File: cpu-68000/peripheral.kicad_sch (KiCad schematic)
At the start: 57 parts, among them J502 DB9_Male_MountingHoles, J503 Conn_02x03_Odd_Even, SW501 SW_DIP_x05, SW502 Blue, SW503 Black, U501 74HC2G14, U502 PCA9543A, U503 XR68C681, U504 PCF8584, U505 DS1744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

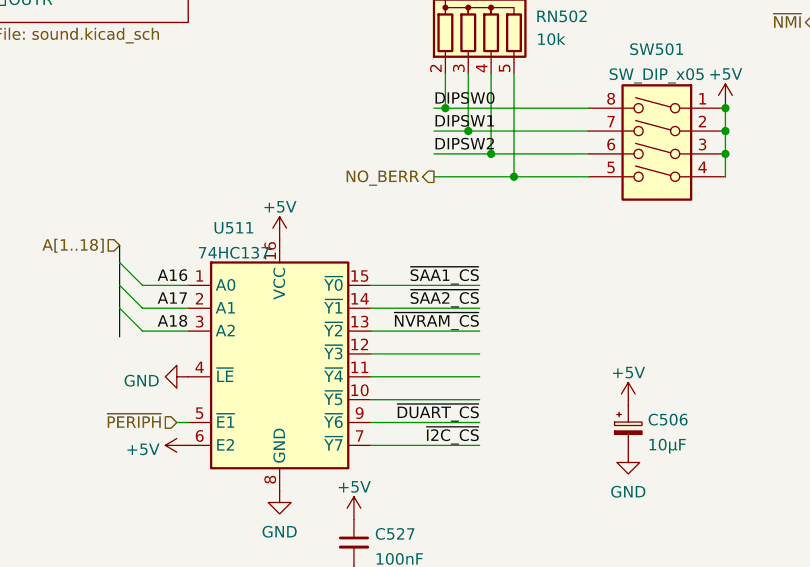
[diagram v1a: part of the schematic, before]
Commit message: Replaced half the RAM for flash (boot ROM)
Squashed commit of the following:

commit 629e5dca317ab35f390a35a51af997ba405215d5
Author: Tristan Seifert <tristan@tseifert.me>
Date:   Tue Nov 30 18:31:19 2021 -0800

    Added high byte flash chip

    - Replaced one of the RAMs with another flash, so that we can have
      on-board boot ROM of 1M. It'll have to be programmed in system (or
      very flimsily out of system before soldering) so a switch to remap the
      flash to elsehwere in the address space is provided (formerly BERR
      inhibit switch)

commit c59845a042d2b99cf0eb5e3cdf44f56cd0b06346
Author: Tristan Seifert <tristan@tseifert.me>
Date:   Tue Nov 30 16:27:37 2021 -0800

    Fixed address line routing to match flash chip

    - While the routing is slightly simplified by having the address lines
      not line up, we instead have the address pins match up so the
      programming logic is simplified (flash can only be written in sectors)

commit c1633293517c92d21a59f13bdb24d4da193bf248
Author: Tristan Seifert <tristan@tseifert.me>
Date:   Tue Nov 30 16:09:11 2021 -0800

    Switched one of the RAMs for a flash chip

    - This should allow us to have a boot ROM on the board; it will need to
      be bootstraped and programmed in-system by some external jig though.

commit 7dedf6a3a6ad9d60be3a7b8b35cf8e3edec37929
Author: Tristan Seifert <tristan@tseifert.me>
Date:   Tue Nov 30 15:02:12 2021 -0800

    Created footprints for PGA 68000

    - Also reworked the address decoding for peripherals so all peripherals
      that generate their own /DTACK are on the same half of the peripheral
      address space
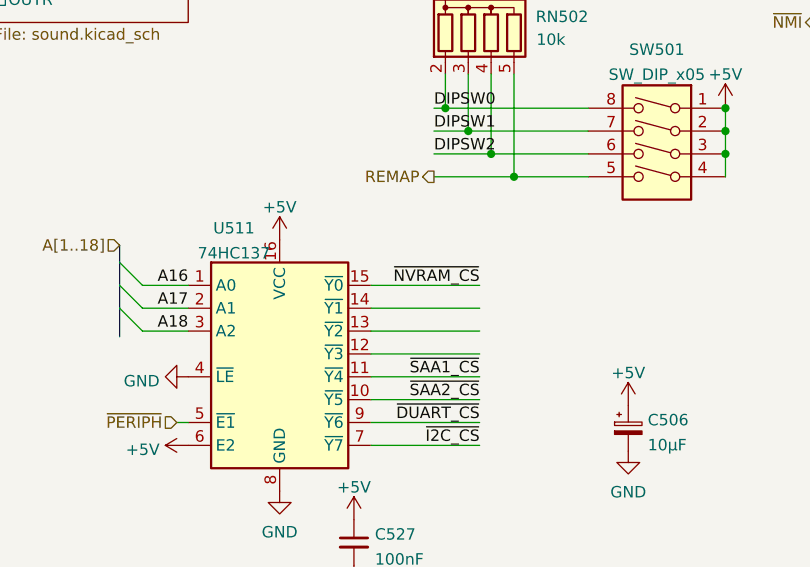
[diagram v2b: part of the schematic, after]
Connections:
- net ~{NVRAM_CS}: now also U511.15 (~{Y0}); no longer U511.13 (~{Y2})
- net ~{SAA1_CS}: now also U511.11 (~{Y4}); no longer U511.15 (~{Y0})
- net ~{SAA2_CS}: now also U511.10 (~{Y5}); no longer U511.14 (~{Y1})
- net NO_BERR renamed REMAP
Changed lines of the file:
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@@
-(kicad_sch (version 20210621) (generator eeschema)
+(kicad_sch (version 20211123) (generator eeschema)
   (paper "A4")
-  (junction (at 156.21 147.955) (diameter 0) (color 0 0 0 0))
-  (junction (at 236.855 124.46) (diameter 0) (color 0 0 0 0))
-  (junction (at 179.705 145.415) (diameter 0) (color 0 0 0 0))
-  (junction (at 170.18 94.615) (diameter 0) (color 0 0 0 0))
-  (junction (at 41.275 151.13) (diameter 0) (color 0 0 0 0))
-  (junction (at 45.72 69.85) (diameter 0) (color 0 0 0 0))
-  (junction (at 45.72 64.77) (diameter 0) (color 0 0 0 0))
-  (junction (at 227.33 124.46) (diameter 0) (color 0 0 0 0))
-  (junction (at 151.13 142.875) (diameter 0) (color 0 0 0 0))
-  (junction (at 212.725 124.46) (diameter 0) (color 0 0 0 0))
-  (junction (at 225.425 99.3624) (diameter 0) (color 0 0 0 0))
-  (junction (at 170.18 99.695) (diameter 0) (color 0 0 0 0))
-  (junction (at 212.725 130.81) (diameter 0) (color 0 0 0 0))
-  (junction (at 77.47 176.53) (diameter 0) (color 0 0 0 0))
-  (junction (at 21.59 81.28) (diameter 0) (color 0 0 0 0))
-  (junction (at 34.925 126.365) (diameter 0) (color 0 0 0 0))
-  (junction (at 179.705 142.875) (diameter 0) (color 0 0 0 0))
-  (junction (at 227.33 140.335) (diameter 0) (color 0 0 0 0))
-  (junction (at 212.725 114.3) (diameter 0) (color 0 0 0 0))
-  (junction (at 41.275 146.05) (diameter 0) (color 0 0 0 0))
-  (junction (at 148.59 140.335) (diameter 0) (color 0 0 0 0))
-  (junction (at 75.565 80.01) (diameter 0) (color 0 0 0 0))
-  (junction (at 151.13 20.955) (diameter 0) (color 0 0 0 0))
-  (junction (at 153.67 145.415) (diameter 0) (color 0 0 0 0))
-  (junction (at 41.275 148.59) (diameter 0) (color 0 0 0 0))
-  (junction (at 41.275 156.21) (diameter 0) (color 0 0 0 0))
-  (junction (at 77.47 181.61) (diameter 0) (color 0 0 0 0))
-  (junction (at 77.47 186.69) (diameter 0) (color 0 0 0 0))
-  (junction (at 273.685 45.72) (diameter 0) (color 0 0 0 0))
-  (junction (at 212.725 140.335) (diameter 0) (color 0 0 0 0))
-  (junction (at 41.275 153.67) (diameter 0) (color 0 0 0 0))
-  (junction (at 179.705 140.335) (diameter 0) (color 0 0 0 0))
-  (junction (at 146.05 20.955) (diameter 0) (color 0 0 0 0))
+  (junction (at 41.275 148.59) (diameter 0) (color 0 0 0 0)
+  )
+  (junction (at 77.47 181.61) (diameter 0) (color 0 0 0 0)
+  )
+  (junction (at 212.725 124.46) (diameter 0) (color 0 0 0 0)
+  )
+  (junction (at 21.59 81.28) (diameter 0) (color 0 0 0 0)
+  )
+  (junction (at 77.47 176.53) (diameter 0) (color 0 0 0 0)
+  )
+  (junction (at 45.72 64.77) (diameter 0) (color 0 0 0 0)
+  )
+  (junction (at 151.13 20.955) (diameter 0) (color 0 0 0 0)
+  )
+  (junction (at 212.725 130.81) (diameter 0) (color 0 0 0 0)
+  )
+  (junction (at 225.425 99.3624) (diameter 0) (color 0 0 0 0)
+  )
+  (junction (at 236.855 124.46) (diameter 0) (color 0 0 0 0)
+  )
+  (junction (at 170.18 94.615) (diameter 0) (color 0 0 0 0)
+  )
+  (junction (at 75.565 80.01) (diameter 0) (color 0 0 0 0)
+  )
+  (junction (at 212.725 140.335) (diameter 0) (color 0 0 0 0)
+  )
+  (junction (at 179.705 142.875) (diameter 0) (color 0 0 0 0)
+  )
+  (junction (at 45.72 69.85) (diameter 0) (color 0 0 0 0)
+  )
+  (junction (at 170.18 99.695) (diameter 0) (color 0 0 0 0)
+  )
+  (junction (at 273.685 45.72) (diameter 0) (color 0 0 0 0)
+  )
+  (junction (at 41.275 146.05) (diameter 0) (color 0 0 0 0)
+  )
+  (junction (at 153.67 145.415) (diameter 0) (color 0 0 0 0)
+  )
+  (junction (at 227.33 140.335) (diameter 0) (color 0 0 0 0)
+  )
+  (junction (at 77.47 186.69) (diameter 0) (color 0 0 0 0)
+  )
+  (junction (at 156.21 147.955) (diameter 0) (color 0 0 0 0)
+  )
+  (junction (at 148.59 140.335) (diameter 0) (color 0 0 0 0)
+  )
+  (junction (at 34.925 126.365) (diameter 0) (color 0 0 0 0)
+  )
+  (junction (at 41.275 151.13) (diameter 0) (color 0 0 0 0)
+  )
+  (junction (at 179.705 145.415) (diameter 0) (color 0 0 0 0)
+  )
+  (junction (at 146.05 20.955) (diameter 0) (color 0 0 0 0)
+  )
+  (junction (at 41.275 153.67) (diameter 0) (color 0 0 0 0)
+  )
+  (junction (at 41.275 156.21) (diameter 0) (color 0 0 0 0)
+  )
+  (junction (at 179.705 140.335) (diameter 0) (color 0 0 0 0)
+  )
+  (junction (at 151.13 142.875) (diameter 0) (color 0 0 0 0)
+  )
+  (junction (at 212.725 114.3) (diameter 0) (color 0 0 0 0)
+  )
+  (junction (at 227.33 124.46) (diameter 0) (color 0 0 0 0)
+  )
   (bus_entry (at 132.715 41.275) (size 2.54 -2.54)
     (stroke (width 0) (type default) (color 0 0 0 0))
@@
     (effects (font (size 1.27 1.27)) (justify right bottom))
   )
-  (label "~{NVRAM_CS}" (at 152.4 165.1 180)
+  (label "~{NVRAM_CS}" (at 152.4 160.02 180)
     (effects (font (size 1.27 1.27)) (justify right bottom))
   )
@@
     (effects (font (size 1.27 1.27)) (justify right bottom))
   )
-  (label "~{SAA2_CS}" (at 152.4 162.56 180)
+  (label "~{SAA2_CS}" (at 152.4 172.72 180)
     (effects (font (size 1.27 1.27)) (justify right bottom))
   )
@@
     (effects (font (size 1.27 1.27)) (justify right bottom))
   )
-  (label "~{SAA1_CS}" (at 152.4 160.02 180)
+  (label "~{SAA1_CS}" (at 152.4 170.18 180)
     (effects (font (size 1.27 1.27)) (justify right bottom))
   )
@@
     (effects (font (size 1.27 1.27)) (justify right))
   )
-  (hierarchical_label "NO_BERR" (shape output) (at 147.32 147.955 180)
-    (effects (font (size 1.27 1.27)) (justify right))
-  )
+  (hierarchical_label "REMAP" (shape output) (at 147.32 147.955 180)
+    (effects (font (size 1.27 1.27)) (justify right))
+  )

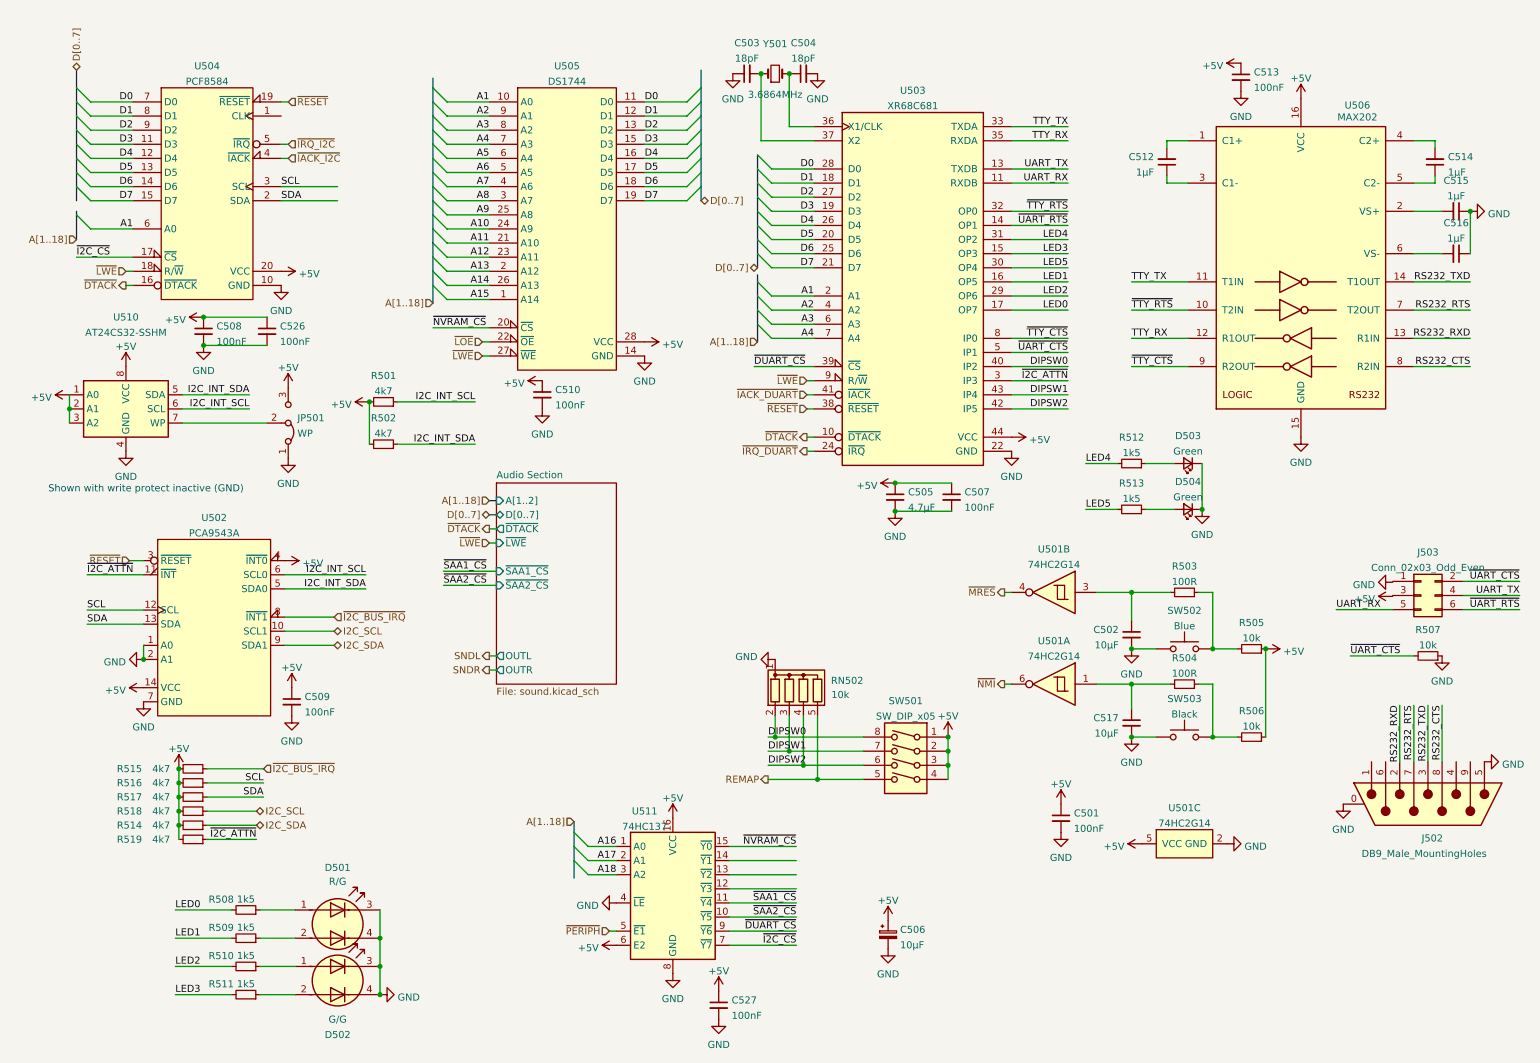
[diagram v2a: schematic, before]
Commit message: Minor cleanup of CPU board
- Switched out of stock 2 bit level shifters for 8 bit part we already
  have; this means that the function codes will be buffered along with
  all other signals.
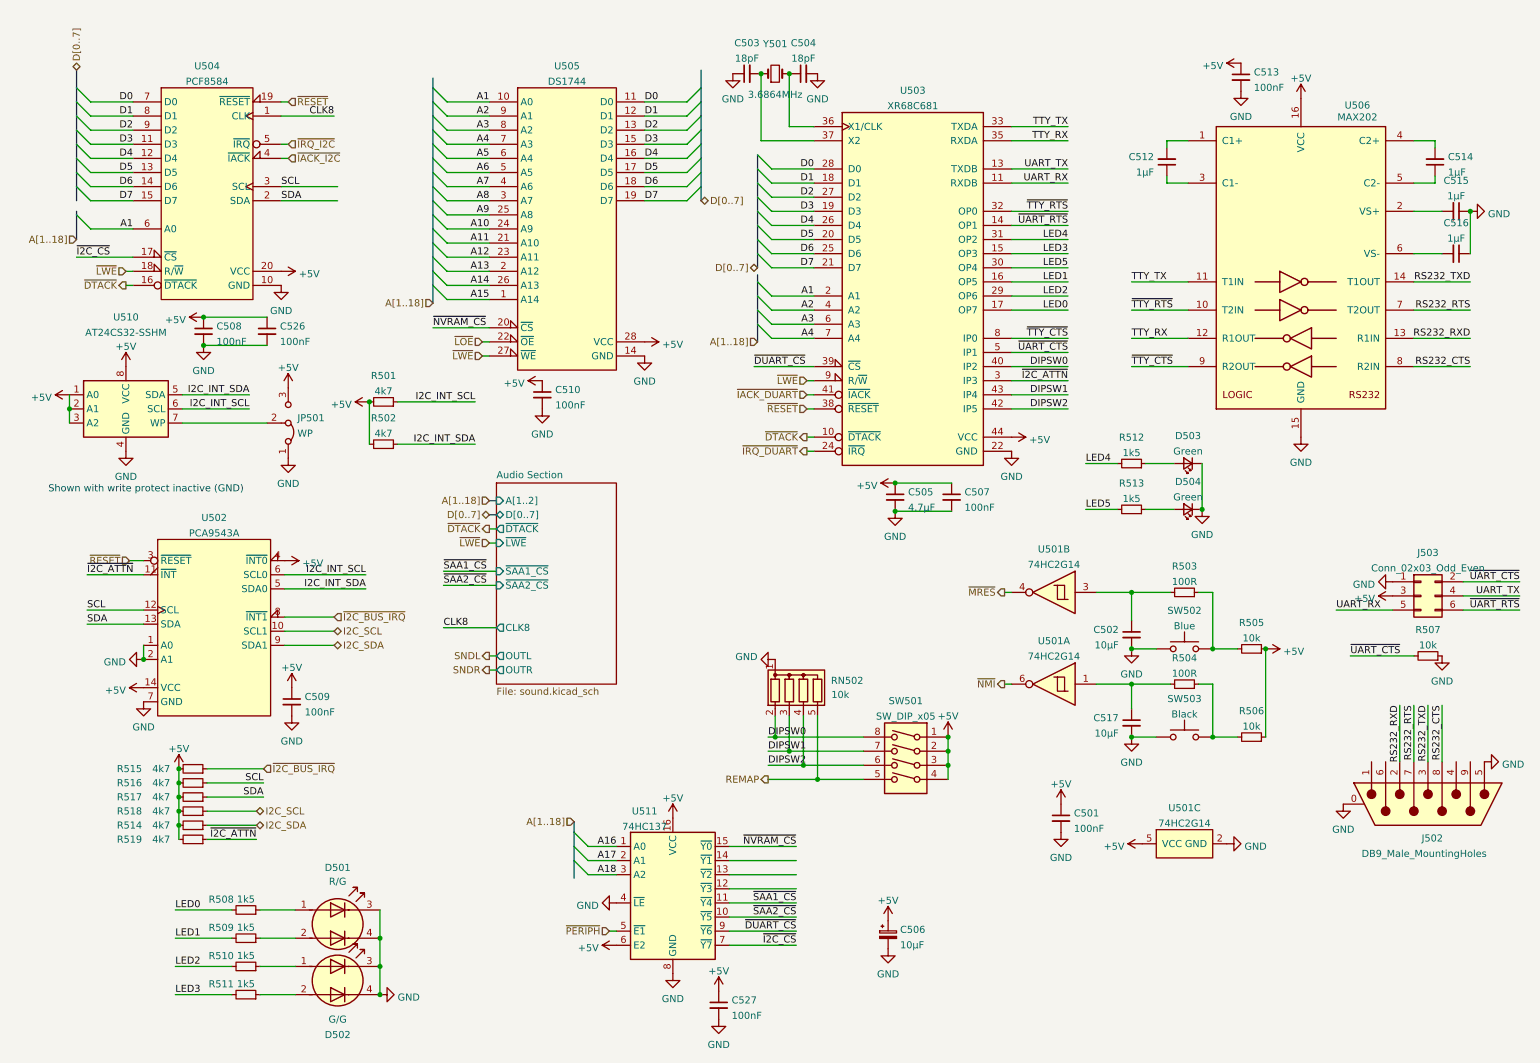
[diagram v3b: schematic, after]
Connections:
- net +5V: now also J503.3 (Pin_3)
- net GND: now also J503.1 (Pin_1)
- net CLK8: now reaches U504.1 (CLK)
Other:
- sheet Audio Section ports: added CLK8; removed none
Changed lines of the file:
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@@
     (stroke (width 0) (type default) (color 0 0 0 0))
   )
-  (wire (pts (xy 272.415 117.3964) (xy 282.575 117.3964))
+  (wire (pts (xy 272.415 117.475) (xy 282.575 117.475))
     (stroke (width 0) (type default) (color 0 0 0 0))
   )
@@
     (stroke (width 0) (type default) (color 0 0 0 0))
   )
-  (wire (pts (xy 272.415 112.3164) (xy 282.575 112.3164))
+  (wire (pts (xy 272.415 112.395) (xy 282.575 112.395))
     (stroke (width 0) (type default) (color 0 0 0 0))
   )
@@
     (stroke (width 0) (type default) (color 0 0 0 0))
   )
+  (wire (pts (xy 88.9 120.65) (xy 98.425 120.65))
+    (stroke (width 0) (type default) (color 0 0 0 0))
+  )
   (wire (pts (xy 125.095 33.655) (xy 132.715 33.655))
     (stroke (width 0) (type default) (color 0 0 0 0))
@@
     (stroke (width 0) (type default) (color 0 0 0 0))
   )
-  (wire (pts (xy 272.415 114.8564) (xy 282.575 114.8564))
+  (wire (pts (xy 272.415 114.935) (xy 282.575 114.935))
     (stroke (width 0) (type default) (color 0 0 0 0))
   )
@@
     (stroke (width 0) (type default) (color 0 0 0 0))
   )
-  (wire (pts (xy 259.715 117.3964) (xy 249.555 117.3964))
+  (wire (pts (xy 259.715 117.475) (xy 249.555 117.475))
     (stroke (width 0) (type default) (color 0 0 0 0))
   )
@@
     (stroke (width 0) (type default) (color 0 0 0 0))
   )
+  (wire (pts (xy 69.215 28.575) (xy 59.69 28.575))
+    (stroke (width 0) (type default) (color 0 0 0 0))
+  )
   (wire (pts (xy 50.8 176.53) (xy 40.64 176.53))
     (stroke (width 0) (type default) (color 0 0 0 0))
@@
     (effects (font (size 1.27 1.27)) (justify right bottom))
   )
-  (label "~{UART_RTS}" (at 282.575 117.3964 180)
+  (label "~{UART_RTS}" (at 282.575 117.475 180)
     (effects (font (size 1.27 1.27)) (justify right bottom))
   )
@@
     (effects (font (size 1.27 1.27)) (justify right bottom))
   )
+  (label "CLK8" (at 88.9 120.65 0)
+    (effects (font (size 1.27 1.27)) (justify left bottom))
+  )
   (label "I2C_INT_SDA" (at 53.975 78.74 180)
     (effects (font (size 1.27 1.27)) (justify right bottom))
@@
     (effects (font (size 1.27 1.27)) (justify right bottom))
   )
-  (label "UART_RX" (at 249.555 117.3964 0)
+  (label "UART_RX" (at 249.555 117.475 0)
     (effects (font (size 1.27 1.27)) (justify left bottom))
   )
@@
     (effects (font (size 1.27 1.27)) (justify right bottom))
   )
+  (label "CLK8" (at 69.215 28.575 180)
+    (effects (font (size 1.27 1.27)) (justify right bottom))
+  )
   (label "~{DUART_CS}" (at 144.78 73.66 0)
     (effects (font (size 1.27 1.27)) (justify left bottom))
@@
     (effects (font (size 1.27 1.27)) (justify right bottom))
   )
-  (label "UART_TX" (at 282.575 114.8564 180)
+  (label "UART_TX" (at 282.575 114.935 180)
     (effects (font (size 1.27 1.27)) (justify right bottom))
   )
@@
     (effects (font (size 1.27 1.27)) (justify right bottom))
   )
-  (label "~{UART_CTS}" (at 282.575 112.3164 180)
+  (label "~{UART_CTS}" (at 282.575 112.395 180)
     (effects (font (size 1.27 1.27)) (justify right bottom))
   )
@@
     (pin "1")
   )
-  (symbol (lib_id "Connector_Generic:Conn_02x03_Odd_Even") (at 264.795 114.8564 0) (unit 1)
+  (symbol (lib_id "Connector_Generic:Conn_02x03_Odd_Even") (at 264.795 114.935 0) (unit 1)
     (in_bom yes) (on_board yes) (fields_autoplaced)
-    (property "Reference" "J503" (id 0) (at 266.065 107.0799 0))
-    (property "Value" "Conn_02x03_Odd_Even" (id 1) (at 266.065 109.855 0))
-    (property "Footprint" "Connector_PinHeader_2.54mm:PinHeader_2x03_P2.54mm_Horizontal" (id 2) (at 264.795 114.8564 0)
+    (property "Reference" "J503" (id 0) (at 266.065 107.1585 0))
+    (property "Value" "Conn_02x03_Odd_Even" (id 1) (at 266.065 109.9336 0))
+    (property "Footprint" "Connector_PinHeader_2.54mm:PinHeader_2x03_P2.54mm_Horizontal" (id 2) (at 264.795 114.935 0)
       (effects (font (size 1.27 1.27)) hide)
     )
-    (property "Datasheet" "~" (id 3) (at 264.795 114.8564 0)
+    (property "Datasheet" "~" (id 3) (at 264.795 114.935 0)
       (effects (font (size 1.27 1.27)) hide)
     )
@@
     (pin "2")
   )
-  (symbol (lib_id "power:GND") (at 259.715 112.4724 270) (unit 1)
+  (symbol (lib_id "power:GND") (at 259.715 112.395 270) (unit 1)
     (in_bom yes) (on_board yes) (fields_autoplaced)
-    (property "Reference" "#PWR0210" (id 0) (at 253.365 112.4724 0)
+    (property "Reference" "#PWR0210" (id 0) (at 253.365 112.395 0)
       (effects (font (size 1.27 1.27)) hide)
     )
-    (property "Value" "GND" (id 1) (at 256.54 112.9514 90)
+    (property "Value" "GND" (id 1) (at 256.54 112.874 90)
       (effects (font (size 1.27 1.27)) (justify right))
     )
-    (property "Footprint" "" (id 2) (at 259.715 112.4724 0)
+    (property "Footprint" "" (id 2) (at 259.715 112.395 0)
       (effects (font (size 1.27 1.27)) hide)
     )
-    (property "Datasheet" "" (id 3) (at 259.715 112.4724 0)
+    (property "Datasheet" "" (id 3) (at 259.715 112.395 0)
       (effects (font (size 1.27 1.27)) hide)
     )
@@
     (pin "1")
   )
-  (symbol (lib_id "power:+5V") (at 259.715 115.0124 90) (unit 1)
+  (symbol (lib_id "power:+5V") (at 259.715 114.935 90) (unit 1)
     (in_bom yes) (on_board yes) (fields_autoplaced)
-    (property "Reference" "#PWR0211" (id 0) (at 263.525 115.0124 0)
+    (property "Reference" "#PWR0211" (id 0) (at 263.525 114.935 0)
       (effects (font (size 1.27 1.27)) hide)
     )
-    (property "Value" "+5V" (id 1) (at 256.54 115.4914 90)
+    (property "Value" "+5V" (id 1) (at 256.54 115.414 90)
       (effects (font (size 1.27 1.27)) (justify left))
     )
-    (property "Footprint" "" (id 2) (at 259.715 115.0124 0)
+    (property "Footprint" "" (id 2) (at 259.715 114.935 0)
       (effects (font (size 1.27 1.27)) hide)
     )
-    (property "Datasheet" "" (id 3) (at 259.715 115.0124 0)
+    (property "Datasheet" "" (id 3) (at 259.715 114.935 0)
       (effects (font (size 1.27 1.27)) hide)
     )
@@
       (effects (font (size 1.27 1.27)) (justify left))
     )
+    (pin "CLK8" output (at 98.425 120.65 180)
+      (effects (font (size 1.27 1.27)) (justify left))
+    )
